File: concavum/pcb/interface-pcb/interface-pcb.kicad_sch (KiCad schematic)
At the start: 9 parts, among them J1 Audio_Jack, J2 FPC_connector, U1 Adafruit_KB2040, U2 MCP23017/MCP23018

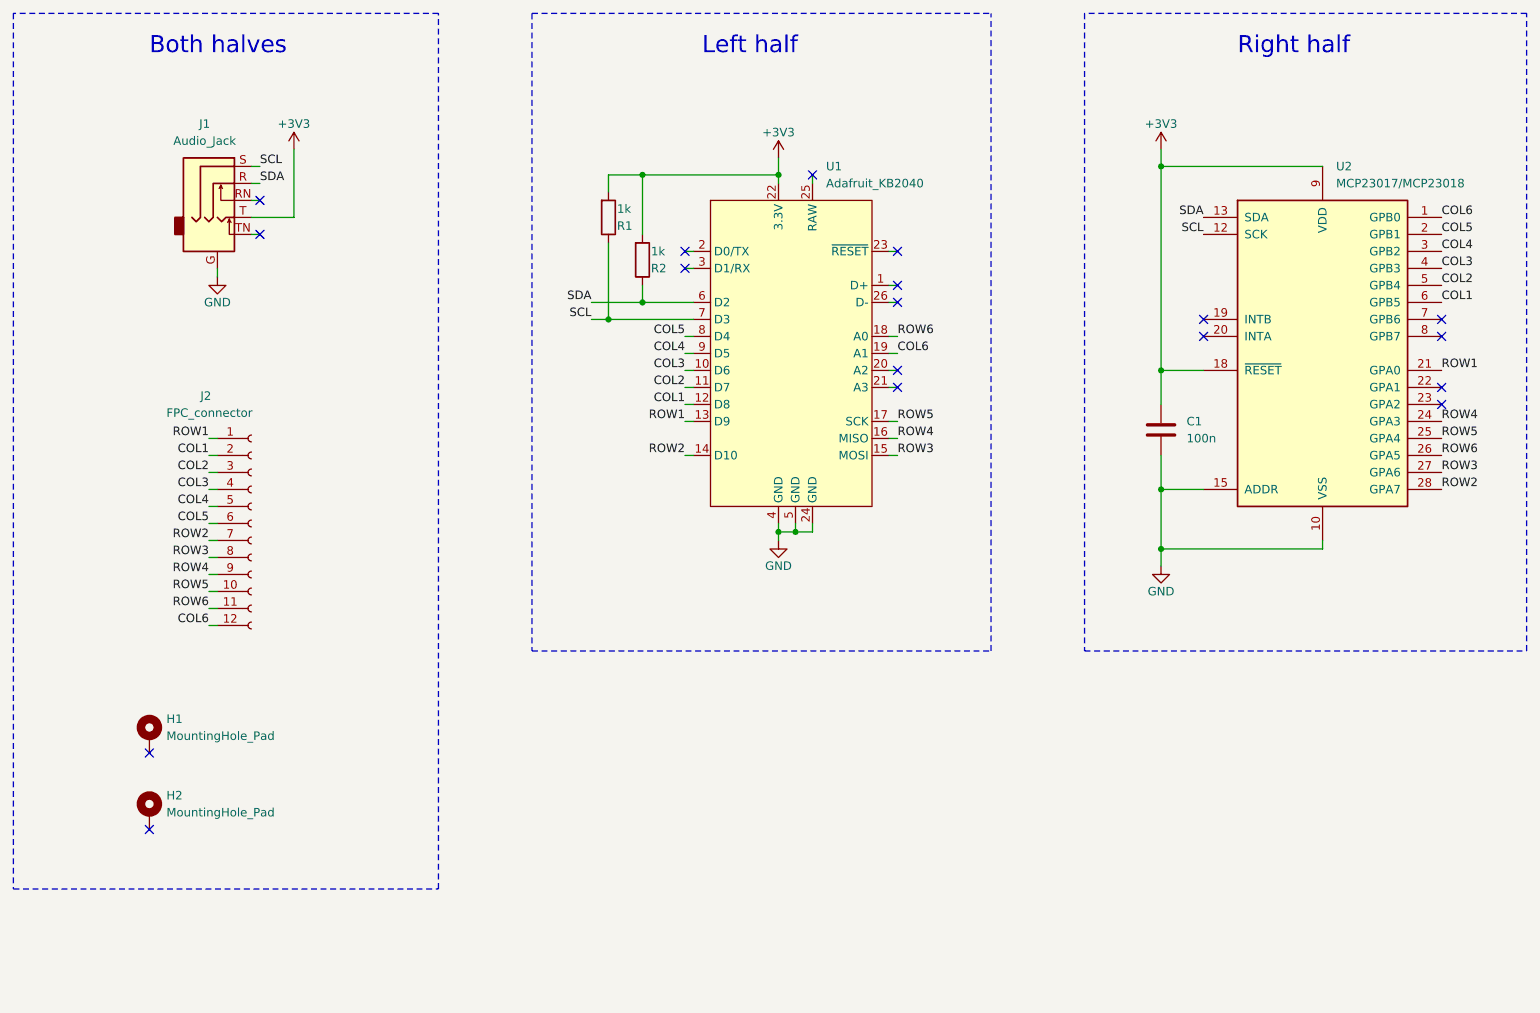
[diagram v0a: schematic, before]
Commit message: Add optional pullup resistors to interface PCB
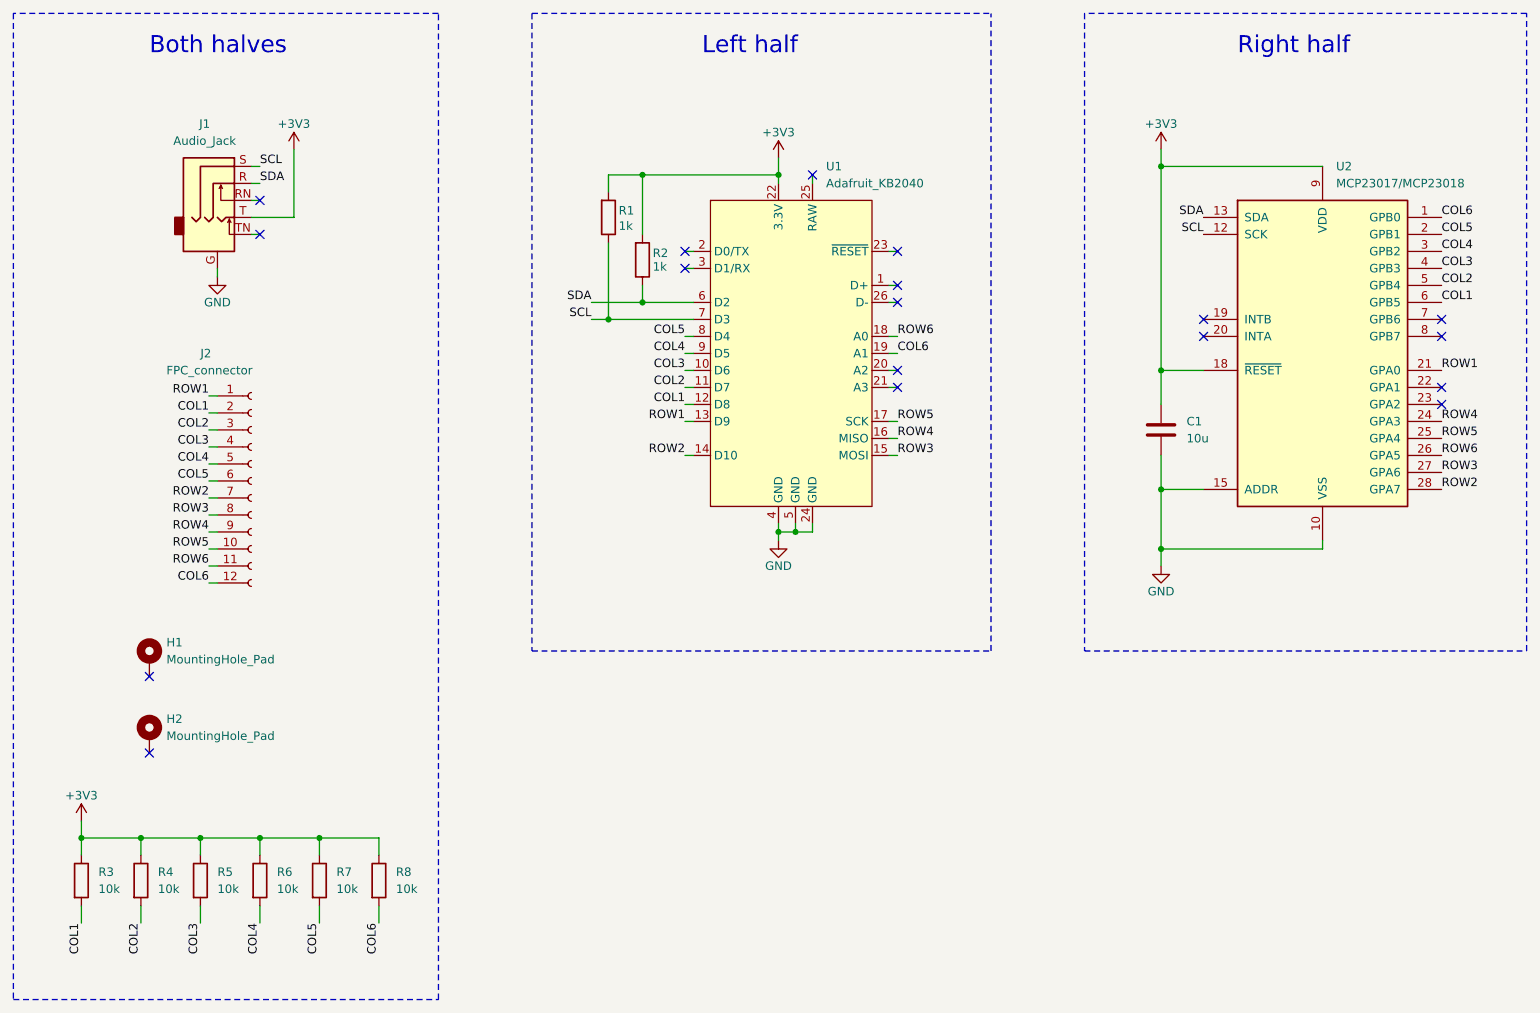
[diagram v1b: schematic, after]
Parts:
- added R3, R4, R5, R6, R7, R8: 10k, Resistor_SMD:R_1206_3216Metric, symbol Device:R
- C1: value 100n -> 10u
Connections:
- net +3V3: now also R3.1, R4.1, R5.1, R6.1, R7.1, R8.1
- net COL1: now also R3.2
- net COL2: now also R4.2
- net COL3: now also R5.2
- net COL4: now also R6.2
- net COL5: now also R7.2
- net COL6: now also R8.2
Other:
- moved on the sheet: H1, H2, J2
